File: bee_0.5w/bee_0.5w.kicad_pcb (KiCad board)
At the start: 2 copper layers, 13.7 x 53.3 mm, 12 parts, among them J1 Conn_01x02_Male, J2 Conn_01x02_Male, J3 Conn_01x02_Male, J4 Conn_01x02_Male

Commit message: Add sch symbols for labels, update PCB accordingly.
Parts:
- removed REF** (x2): Text_U_B+_Silkscreen, Symbol-emt:Text_U_B+_Silkscreen
- removed REF** (x2): Text_U_B-_Silkscreen, Symbol-emt:Text_U_B-_Silkscreen
- removed REF** (x2): Text_U_B2_Silkscreen, Symbol-emt:Text_U_B2_Silkscreen
- removed REF** (x2): Symbol_GND_Silkscreen, Symbol-emt:Symbol_GND_Silkscreen
- added H1: Silkscreen_Label, Symbol-emt:Text_U_B+_Silkscreen, F.Cu at (75.2, 91.4)
- added H2: Silkscreen_Label, Symbol-emt:Text_U_B+_Silkscreen, F.Cu at (85.9, 91.4)
- added H3: Silkscreen_Label, Symbol-emt:Text_U_B-_Silkscreen, F.Cu at (75.2, 94.0)
- added H4: Silkscreen_Label, Symbol-emt:Text_U_B-_Silkscreen, F.Cu at (85.9, 94.0)
- added H5: Silkscreen_Label, Symbol-emt:Text_U_B2_Silkscreen, F.Cu at (75.2, 137.2)
- added H6: Silkscreen_Label, Symbol-emt:Text_U_B2_Silkscreen, F.Cu at (85.9, 137.2)
- added H7: Silkscreen_Label, Symbol-emt:Symbol_GND_Silkscreen, F.Cu at (75.7, 139.7)
- added H8: Silkscreen_Label, Symbol-emt:Symbol_GND_Silkscreen, F.Cu at (86.9, 139.7)
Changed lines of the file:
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@@
-(kicad_pcb (version 20171130) (host pcbnew 5.0.2+dfsg1-1~bpo9+1)
+(kicad_pcb (version 20171130) (host pcbnew "(5.1.0)-1")
   (general
     (thickness 1.6)
@@
     (zone_45_only no)
     (trace_min 0.2)
-    (segment_width 0.2)
-    (edge_width 0.15)
     (via_size 0.8)
     (via_drill 0.4)
@@
     (uvia_min_size 0.2)
     (uvia_min_drill 0.1)
+    (edge_width 0.15)
+    (segment_width 0.2)
     (pcb_text_width 0.3)
     (pcb_text_size 1.5 1.5)
@@
     (solder_mask_min_width 0.25)
     (aux_axis_origin 0 0)
-    (visible_elements FFFFFF7F)
+    (visible_elements 7FFFFFFF)
     (pcbplotparams
       (layerselection 0x010fc_ffffffff)
@@
     (tags "Voltage Label Betriebsspannung")
     (attr virtual)
-    (fp_text reference REF** (at 0 1.65) (layer F.SilkS) hide
-      (effects (font (size 1 1) (thickness 0.15)))
-    )
-    (fp_text value Text_U_B+_Silkscreen (at 0 -1.5) (layer F.Fab) hide
+    (fp_text reference H1 (at 0 1.65) (layer F.SilkS) hide
+      (effects (font (size 1 1) (thickness 0.15)))
+    )
+    (fp_text value Silkscreen_Label (at 0 -1.5) (layer F.Fab) hide
       (effects (font (size 1 1) (thickness 0.15)))
     )
@@
     (fp_text user U (at 0 0) (layer F.SilkS)
       (effects (font (size 1 1) (thickness 0.15)))
+    )
+  )
+  (module Symbol-emt:Text_U_B+_Silkscreen (layer F.Cu)
+    (at 85.852 91.44)
+    (descr "Voltage Label Betriebsspannung")
+    (tags "Voltage Label Betriebsspannung")
+    (attr virtual)
+    (fp_text reference H2 (at 0 1.65) (layer F.SilkS) hide
+      (effects (font (size 1 1) (thickness 0.15)))
+    )
+    (fp_text value Silkscreen_Label (at 0 -1.5) (layer F.Fab) hide
+      (effects (font (size 1 1) (thickness 0.15)))
+    )
+    (fp_text user U (at 0 0) (layer F.SilkS)
+      (effects (font (size 1 1) (thickness 0.15)))
+    )
+    (fp_text user B+ (at 1.2 0.5) (layer F.SilkS)
+      (effects (font (size 0.7 0.7) (thickness 0.1)))
     )
   )
@@
     (tags "Voltage Label Betriebsspannung")
     (attr virtual)
-    (fp_text reference REF** (at 0 1.65) (layer F.SilkS) hide
-      (effects (font (size 1 1) (thickness 0.15)))
-    )
-    (fp_text value Text_U_B-_Silkscreen (at 0 -1.5) (layer F.Fab) hide
+    (fp_text reference H3 (at 0 1.65) (layer F.SilkS) hide
+      (effects (font (size 1 1) (thickness 0.15)))
+    )
+    (fp_text value Silkscreen_Label (at 0 -1.5) (layer F.Fab) hide
       (effects (font (size 1 1) (thickness 0.15)))
     )
     (fp_text user B- (at 1.2 0.5) (layer F.SilkS)
-      (effects (font (size 0.7 0.7) (thickness 0.1)))
-    )
-    (fp_text user U (at 0 0) (layer F.SilkS)
-      (effects (font (size 1 1) (thickness 0.15)))
-    )
-  )
-  (module Symbol-emt:Text_U_B+_Silkscreen (layer F.Cu)
-    (at 85.852 91.44)
-    (descr "Voltage Label Betriebsspannung")
-    (tags "Voltage Label Betriebsspannung")
-    (attr virtual)
-    (fp_text reference REF** (at 0 1.65) (layer F.SilkS) hide
-      (effects (font (size 1 1) (thickness 0.15)))
-    )
-    (fp_text value Text_U_B+_Silkscreen (at 0 -1.5) (layer F.Fab) hide
-      (effects (font (size 1 1) (thickness 0.15)))
-    )
-    (fp_text user B+ (at 1.2 0.5) (layer F.SilkS)
       (effects (font (size 0.7 0.7) (thickness 0.1)))
     )
@@
     (tags "Voltage Label Betriebsspannung")
     (attr virtual)
-    (fp_text reference REF** (at 0 1.65) (layer F.SilkS) hide
-      (effects (font (size 1 1) (thickness 0.15)))
-    )
-    (fp_text value Text_U_B-_Silkscreen (at 0 -1.5) (layer F.Fab) hide
+    (fp_text reference H4 (at 0 1.65) (layer F.SilkS) hide
+      (effects (font (size 1 1) (thickness 0.15)))
+    )
+    (fp_text value Silkscreen_Label (at 0 -1.5) (layer F.Fab) hide
+      (effects (font (size 1 1) (thickness 0.15)))
+    )
+    (fp_text user U (at 0 0) (layer F.SilkS)
       (effects (font (size 1 1) (thickness 0.15)))
     )
     (fp_text user B- (at 1.2 0.5) (layer F.SilkS)
       (effects (font (size 0.7 0.7) (thickness 0.1)))
-    )
-    (fp_text user U (at 0 0) (layer F.SilkS)
-      (effects (font (size 1 1) (thickness 0.15)))
     )
   )
@@
     (tags "Voltage Label Betriebsspannung")
     (attr virtual)
-    (fp_text reference REF** (at 0 1.65) (layer F.SilkS) hide
-      (effects (font (size 1 1) (thickness 0.15)))
-    )
-    (fp_text value Text_U_B2_Silkscreen (at 0 -1.5) (layer F.Fab) hide
+    (fp_text reference H5 (at 0 1.65) (layer F.SilkS) hide
+      (effects (font (size 1 1) (thickness 0.15)))
+    )
+    (fp_text value Silkscreen_Label (at 0 -1.5) (layer F.Fab) hide
       (effects (font (size 1 1) (thickness 0.15)))
     )
@@
     (fp_text user U (at 0 0) (layer F.SilkS)
       (effects (font (size 1 1) (thickness 0.15)))
+    )
+  )
+  (module Symbol-emt:Text_U_B2_Silkscreen (layer F.Cu)
+    (at 85.852 137.16)
+    (descr "Voltage Label Betriebsspannung")
+    (tags "Voltage Label Betriebsspannung")
+    (attr virtual)
+    (fp_text reference H6 (at 0 1.65) (layer F.SilkS) hide
+      (effects (font (size 1 1) (thickness 0.15)))
+    )
+    (fp_text value Silkscreen_Label (at 0 -1.5) (layer F.Fab) hide
+      (effects (font (size 1 1) (thickness 0.15)))
+    )
+    (fp_text user U (at 0 0) (layer F.SilkS)
+      (effects (font (size 1 1) (thickness 0.15)))
+    )
+    (fp_text user B2 (at 1.1 0.5) (layer F.SilkS)
+      (effects (font (size 0.7 0.7) (thickness 0.1)))
     )
   )
@@
     (tags "Symbol GND")
     (attr virtual)
-    (fp_text reference REF** (at 0 1.6) (layer F.SilkS) hide
-      (effects (font (size 1 1) (thickness 0.15)))
-    )
-    (fp_text value Symbol_GND_Silkscreen (at 0 -0.75) (layer F.Fab) hide
+    (fp_text reference H7 (at 0 1.6) (layer F.SilkS) hide
+      (effects (font (size 1 1) (thickness 0.15)))
+    )
+    (fp_text value Silkscreen_Label (at 0 -0.75) (layer F.Fab) hide
       (effects (font (size 1 1) (thickness 0.15)))
     )
@@
     (tags "Symbol GND")
     (attr virtual)
-    (fp_text reference REF** (at 0 1.6) (layer F.SilkS) hide
-      (effects (font (size 1 1) (thickness 0.15)))
-    )
-    (fp_text value Symbol_GND_Silkscreen (at 0 -0.75) (layer F.Fab) hide
-      (effects (font (size 1 1) (thickness 0.15)))
-    )
+    (fp_text reference H8 (at 0 1.6) (layer F.SilkS) hide
+      (effects (font (size 1 1) (thickness 0.15)))
+    )
+    (fp_text value Silkscreen_Label (at 0 -0.75) (layer F.Fab) hide
+      (effects (font (size 1 1) (thickness 0.15)))
+    )
+    (fp_line (start -0.5 0.8) (end 0.5 0.8) (layer F.SilkS) (width 0.25))
     (fp_line (start 0 0.8) (end 0 0) (layer F.SilkS) (width 0.15))
-    (fp_line (start -0.5 0.8) (end 0.5 0.8) (layer F.SilkS) (width 0.25))
-  )
-  (module Symbol-emt:Text_U_B2_Silkscreen (layer F.Cu)
-    (at 85.852 137.16)
-    (descr "Voltage Label Betriebsspannung")
-    (tags "Voltage Label Betriebsspannung")
-    (attr virtual)
-    (fp_text reference REF** (at 0 1.65) (layer F.SilkS) hide
-      (effects (font (size 1 1) (thickness 0.15)))
-    )
-    (fp_text value Text_U_B2_Silkscreen (at 0 -1.5) (layer F.Fab) hide
-      (effects (font (size 1 1) (thickness 0.15)))
-    )
-    (fp_text user B2 (at 1.1 0.5) (layer F.SilkS)
-      (effects (font (size 0.7 0.7) (thickness 0.1)))
-    )
-    (fp_text user U (at 0 0) (layer F.SilkS)
-      (effects (font (size 1 1) (thickness 0.15)))
-    )
   )
   (gr_line (start 88.138 88.9) (end 88.138 142.24) (layer Edge.Cuts) (width 0.15))

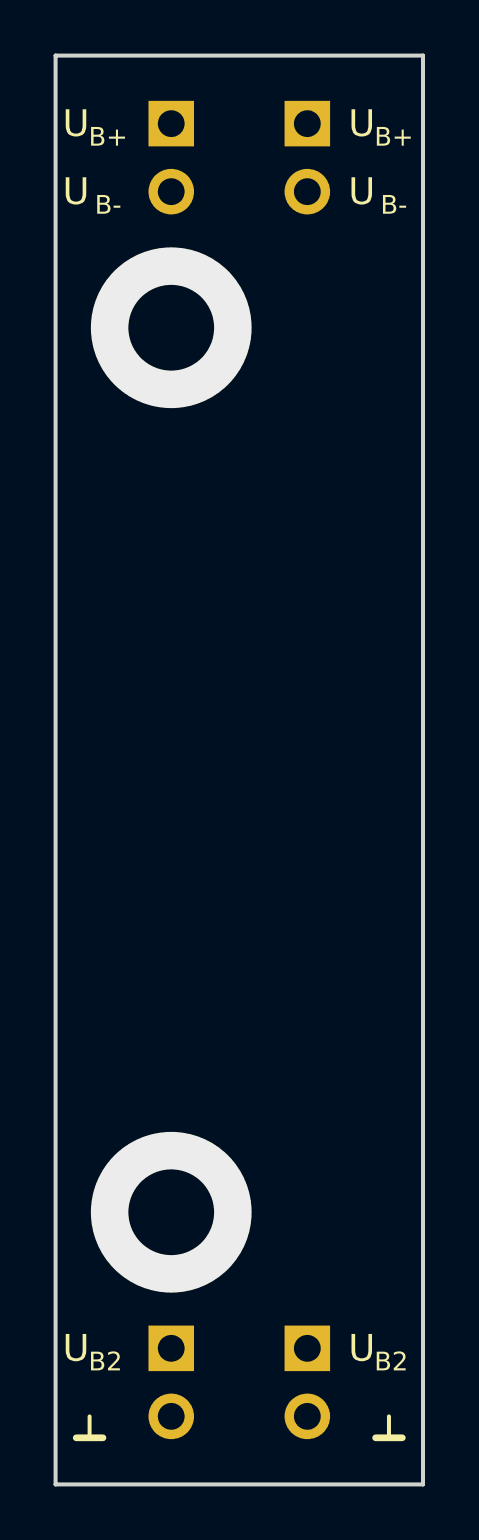
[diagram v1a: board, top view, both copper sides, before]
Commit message: Replace vias by mounting holes.
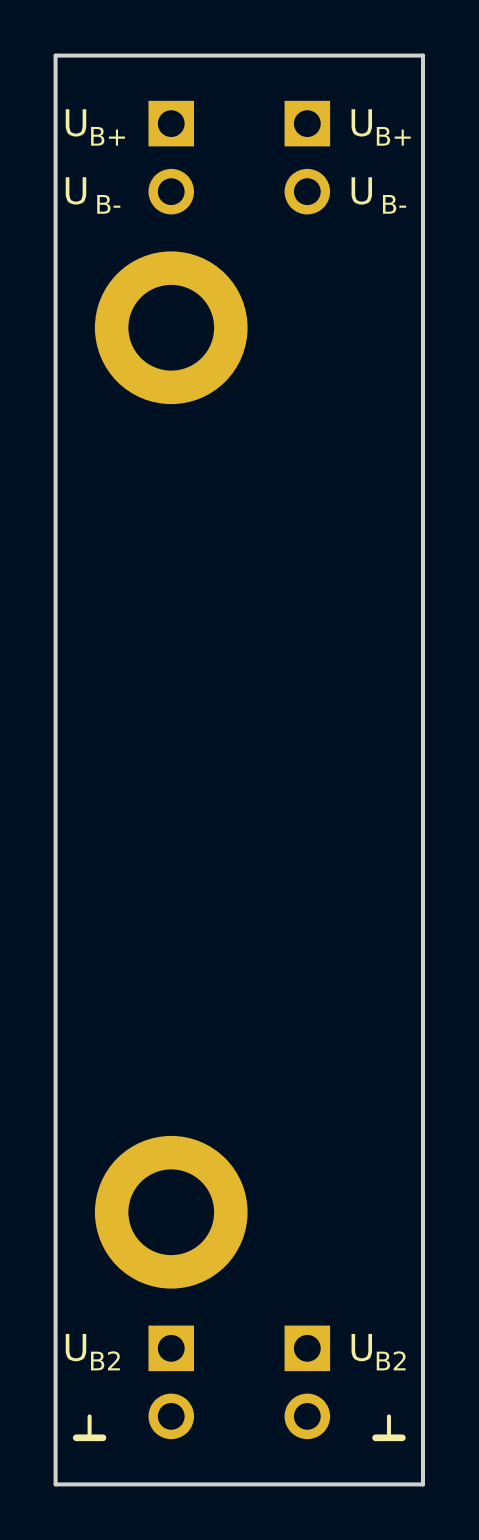
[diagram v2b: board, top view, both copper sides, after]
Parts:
- added H10: MountingHole_Pad, MountingHole:MountingHole_3.2mm_M3_ISO7380_Pad, F.Cu at (78.7, 132.1)
- added H9: MountingHole_Pad, MountingHole:MountingHole_3.2mm_M3_ISO7380_Pad, F.Cu at (78.7, 99.1)
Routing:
- net (no net): vias 2 -> 0
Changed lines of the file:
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@@
     (thickness 1.6)
     (drawings 4)
-    (tracks 2)
+    (tracks 0)
     (zones 0)
-    (modules 12)
+    (modules 14)
     (nets 5)
   )
@@
     (fp_line (start 0 0.8) (end 0 0) (layer F.SilkS) (width 0.15))
   )
+  (module MountingHole:MountingHole_3.2mm_M3_ISO7380_Pad locked (layer F.Cu)
+    (at 78.74 99.06)
+    (descr "Mounting Hole 3.2mm, M3, ISO7380")
+    (tags "mounting hole 3.2mm m3 iso7380")
+    (attr virtual)
+    (fp_text reference H9 (at 0 -3.85) (layer F.SilkS) hide
+      (effects (font (size 1 1) (thickness 0.15)))
+    )
+    (fp_text value MountingHole_Pad (at 0 3.85) (layer F.Fab)
+      (effects (font (size 1 1) (thickness 0.15)))
+    )
+    (fp_circle (center 0 0) (end 3.1 0) (layer F.CrtYd) (width 0.05))
+    (fp_circle (center 0 0) (end 2.85 0) (layer Cmts.User) (width 0.15))
+    (fp_text user %R (at 0.3 0) (layer F.Fab)
+      (effects (font (size 1 1) (thickness 0.15)))
+    )
+    (pad 1 thru_hole circle (at 0 0) (size 5.7 5.7) (drill 3.2) (layers *.Cu *.Mask)
+      (net 3 GND))
+  )
+  (module MountingHole:MountingHole_3.2mm_M3_ISO7380_Pad locked (layer F.Cu)
+    (at 78.74 132.08)
+    (descr "Mounting Hole 3.2mm, M3, ISO7380")
+    (tags "mounting hole 3.2mm m3 iso7380")
+    (attr virtual)
+    (fp_text reference H10 (at 0 -3.85) (layer F.SilkS) hide
+      (effects (font (size 1 1) (thickness 0.15)))
+    )
+    (fp_text value MountingHole_Pad (at 0 3.85) (layer F.Fab)
+      (effects (font (size 1 1) (thickness 0.15)))
+    )
+    (fp_text user %R (at 0.3 0) (layer F.Fab)
+      (effects (font (size 1 1) (thickness 0.15)))
+    )
+    (fp_circle (center 0 0) (end 2.85 0) (layer Cmts.User) (width 0.15))
+    (fp_circle (center 0 0) (end 3.1 0) (layer F.CrtYd) (width 0.05))
+    (pad 1 thru_hole circle (at 0 0) (size 5.7 5.7) (drill 3.2) (layers *.Cu *.Mask)
+      (net 3 GND))
+  )
   (gr_line (start 88.138 88.9) (end 88.138 142.24) (layer Edge.Cuts) (width 0.15))
   (gr_line (start 74.422 142.24) (end 88.138 142.24) (layer Edge.Cuts) (width 0.15))
   (gr_line (start 74.422 88.9) (end 88.138 88.9) (layer Edge.Cuts) (width 0.15))
   (gr_line (start 74.422 88.9) (end 74.422 142.24) (layer Edge.Cuts) (width 0.15))
-  (via (at 78.74 99.06) (size 6) (drill 3.2) (layers F.Cu B.Cu) (net 0) (status 40000))
-  (via (at 78.74 132.08) (size 6) (drill 3.2) (layers F.Cu B.Cu) (net 0) (status 40000))
 )

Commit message: Relabel as bee specific.
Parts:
- H1, H2: footprint Symbol-emt:Text_U_B+_Silkscreen -> Symbol-bee:Text_U_B+_Silkscreen
- H3, H4: footprint Symbol-emt:Text_U_B-_Silkscreen -> Symbol-bee:Text_U_B-_Silkscreen
- H5, H6: footprint Symbol-emt:Text_U_B2_Silkscreen -> Symbol-bee:Text_U_B2_Silkscreen
- H7, H8: footprint Symbol-emt:Symbol_GND_Silkscreen -> Symbol-bee:Symbol_GND_Silkscreen
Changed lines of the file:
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@@
     )
   )
-  (module Symbol-emt:Text_U_B+_Silkscreen (layer F.Cu)
+  (module Symbol-bee:Text_U_B+_Silkscreen (layer F.Cu)
     (at 75.184 91.44)
     (descr "Voltage Label Betriebsspannung")
@@
     )
   )
-  (module Symbol-emt:Text_U_B+_Silkscreen (layer F.Cu)
+  (module Symbol-bee:Text_U_B+_Silkscreen (layer F.Cu)
     (at 85.852 91.44)
     (descr "Voltage Label Betriebsspannung")
@@
     )
   )
-  (module Symbol-emt:Text_U_B-_Silkscreen (layer F.Cu)
+  (module Symbol-bee:Text_U_B-_Silkscreen (layer F.Cu)
     (at 75.184 93.98)
     (descr "Voltage Label Betriebsspannung")
@@
     )
   )
-  (module Symbol-emt:Text_U_B-_Silkscreen (layer F.Cu)
+  (module Symbol-bee:Text_U_B-_Silkscreen (layer F.Cu)
     (at 85.852 93.98)
     (descr "Voltage Label Betriebsspannung")
@@
     )
   )
-  (module Symbol-emt:Text_U_B2_Silkscreen (layer F.Cu)
+  (module Symbol-bee:Text_U_B2_Silkscreen (layer F.Cu)
     (at 75.184 137.16)
     (descr "Voltage Label Betriebsspannung")
@@
     )
   )
-  (module Symbol-emt:Text_U_B2_Silkscreen (layer F.Cu)
+  (module Symbol-bee:Text_U_B2_Silkscreen (layer F.Cu)
     (at 85.852 137.16)
     (descr "Voltage Label Betriebsspannung")
@@
     )
   )
-  (module Symbol-emt:Symbol_GND_Silkscreen (layer F.Cu)
+  (module Symbol-bee:Symbol_GND_Silkscreen (layer F.Cu)
     (at 75.692 139.7)
     (descr "Symbol GND")
@@
     (fp_line (start -0.5 0.8) (end 0.5 0.8) (layer F.SilkS) (width 0.25))
   )
-  (module Symbol-emt:Symbol_GND_Silkscreen (layer F.Cu)
+  (module Symbol-bee:Symbol_GND_Silkscreen (layer F.Cu)
     (at 86.868 139.7)
     (descr "Symbol GND")
